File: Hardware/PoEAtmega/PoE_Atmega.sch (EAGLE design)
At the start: 59 parts, among them IC2 ATMEGA32U4-MU, U2 SPX3819-3.3, U4 W5500, X1 J1011F21P, X3 microUSB, Y2 CRYSTAL-GROUNDEDSMD-3.2X2.5, Y4 8MHz

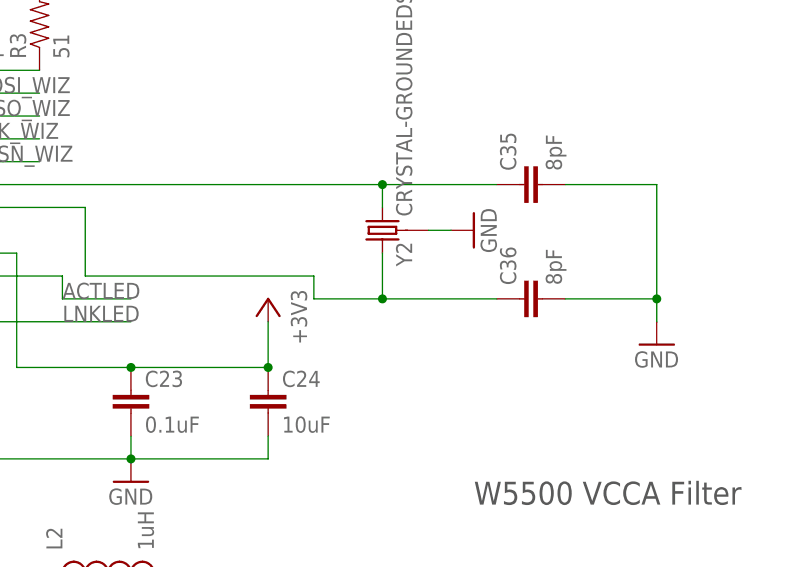
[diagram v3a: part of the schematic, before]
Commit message: HEEP-508 added 25mhz value to wiznet xtal
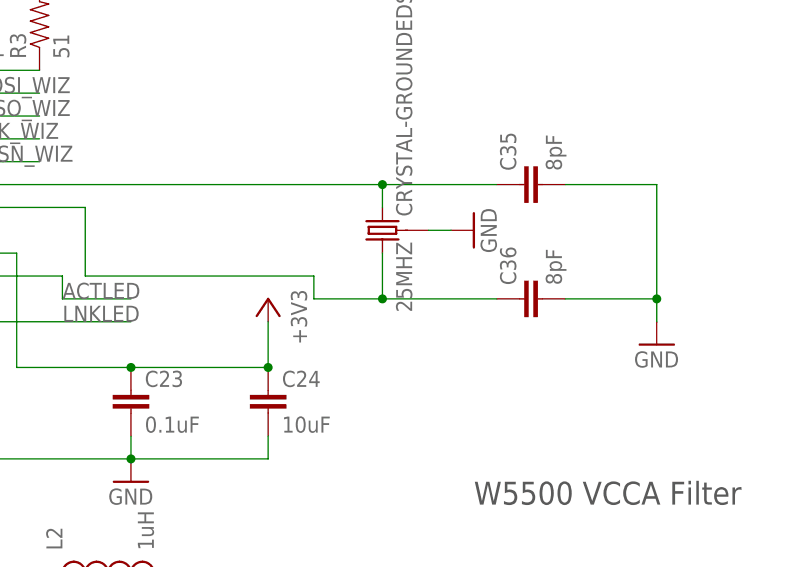
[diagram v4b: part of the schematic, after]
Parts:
- renumbered Y2 to 25MHZ
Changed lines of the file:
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@@
 <part name="GND30" library="SparkFun-Aesthetics" deviceset="GND" device=""/>
 <part name="GND33" library="SparkFun-Aesthetics" deviceset="GND" device=""/>
-<part name="Y2" library="SparkFun-Clocks" deviceset="CRYSTAL-GROUNDED" device="SMD-3.2X2.5"/>
+<part name="25MHZ" library="SparkFun-Clocks" deviceset="CRYSTAL-GROUNDED" device="SMD-3.2X2.5"/>
 <part name="GND36" library="SparkFun-Aesthetics" deviceset="GND" device=""/>
 <part name="C9" library="SparkFun-Passives" deviceset="CAP" device="0603-CAP" value="0.1uF"/>
@@
 <instance part="GND30" gate="1" x="142.24" y="-5.08"/>
 <instance part="GND33" gate="1" x="210.82" y="58.42"/>
-<instance part="Y2" gate="G$1" x="236.22" y="116.84" rot="R90"/>
+<instance part="25MHZ" gate="G$1" x="236.22" y="116.84" rot="R90"/>
 <instance part="GND36" gate="1" x="246.38" y="116.84" rot="R90"/>
 <instance part="C9" gate="G$1" x="243.84" y="68.58"/>
@@
 </segment>
 <segment>
-<pinref part="Y2" gate="G$1" pin="3"/>
+<pinref part="25MHZ" gate="G$1" pin="3"/>
 <pinref part="GND36" gate="1" pin="GND"/>
 <wire x1="243.84" y1="116.84" x2="241.3" y2="116.84" width="0.1524" layer="91"/>
@@
 <pinref part="C35" gate="G$1" pin="1"/>
 <wire x1="187.96" y1="121.92" x2="236.22" y2="121.92" width="0.1524" layer="91"/>
-<pinref part="Y2" gate="G$1" pin="2"/>
+<pinref part="25MHZ" gate="G$1" pin="2"/>
 <wire x1="236.22" y1="121.92" x2="248.92" y2="121.92" width="0.1524" layer="91"/>
 <wire x1="236.22" y1="119.38" x2="236.22" y2="121.92" width="0.1524" layer="91"/>
@@
 <segment>
 <pinref part="C36" gate="G$1" pin="1"/>
-<pinref part="Y2" gate="G$1" pin="1"/>
+<pinref part="25MHZ" gate="G$1" pin="1"/>
 <wire x1="248.92" y1="109.22" x2="236.22" y2="109.22" width="0.1524" layer="91"/>
 <wire x1="236.22" y1="109.22" x2="236.22" y2="114.3" width="0.1524" layer="91"/>
